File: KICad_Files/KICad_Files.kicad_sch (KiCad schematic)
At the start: 48 parts, among them J1 Conn_01x03_MountingPin, J10 Conn_01x03_Pin, J2 USB_C_Receptacle_USB2.0_14P, J3 Conn_01x03_MountingPin, J4 Conn_01x03_MountingPin, J5 Conn_01x03_Pin, J6 Conn_01x06, J7 Conn_01x06, J8 Conn_01x03_Pin, J9 Conn_01x02_Pin, SW1 Reset, SW2 Boot, U1 ESP32-C3, U2 USBLC6-2SC6, U3 TPP361061-T6TR, Y1 40.0MHz

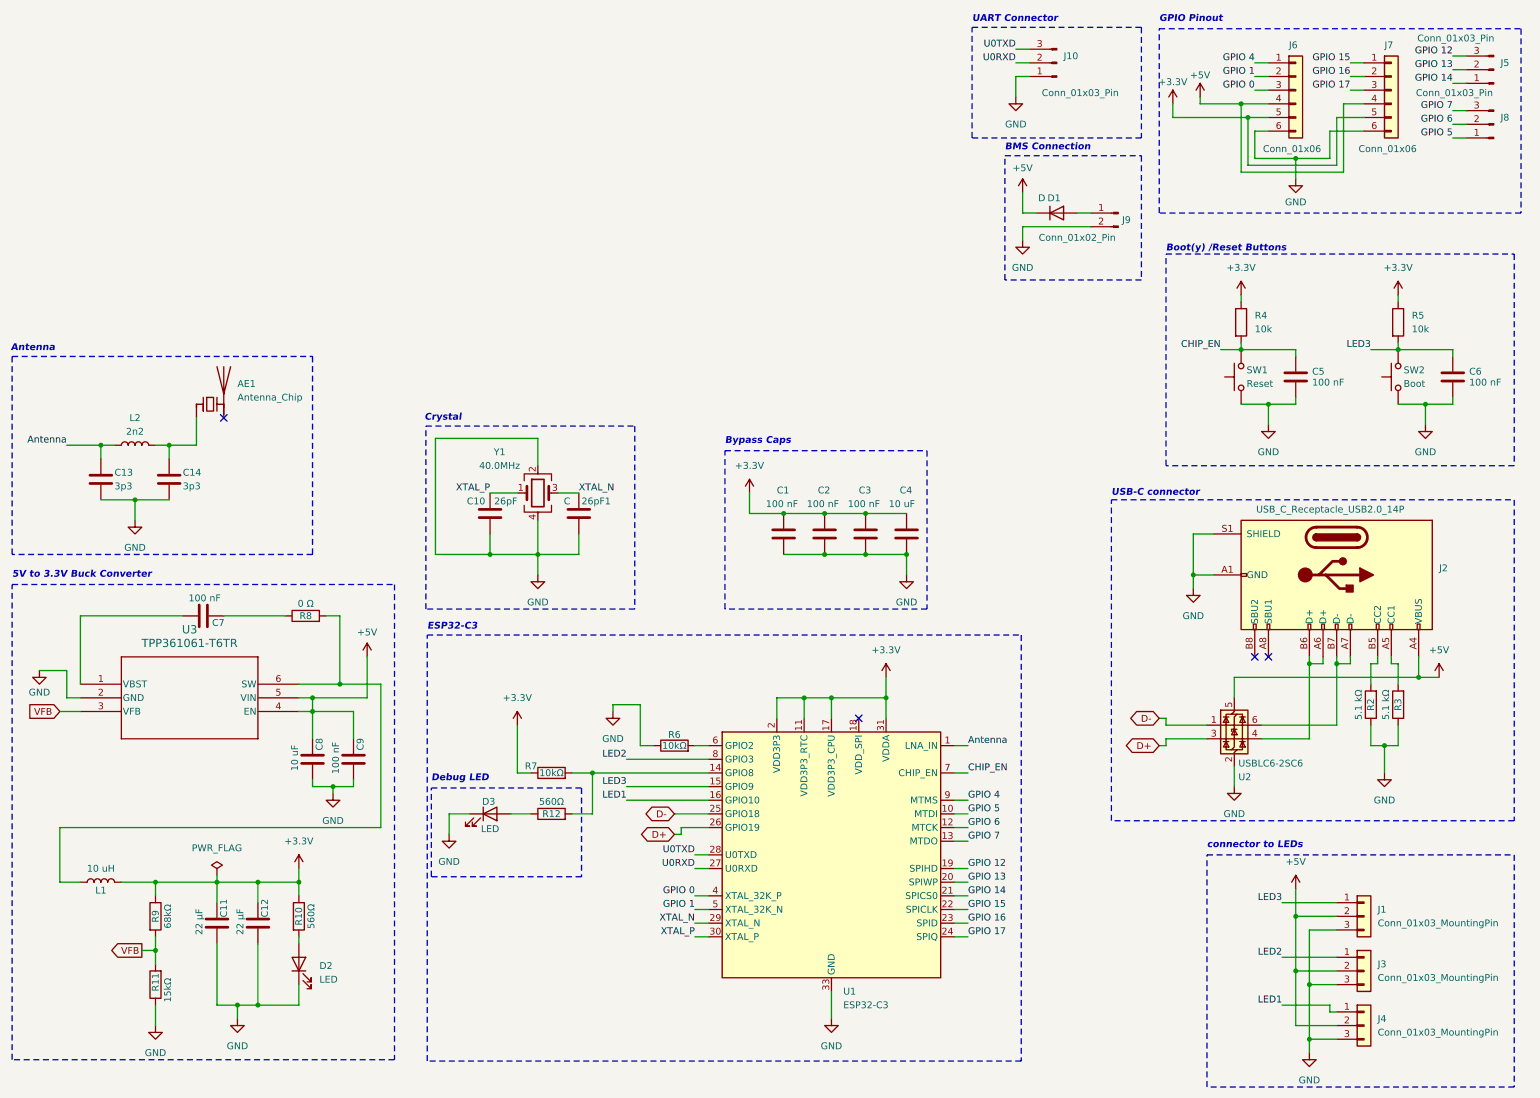
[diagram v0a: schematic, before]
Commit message: Complete rework of the PCB routing
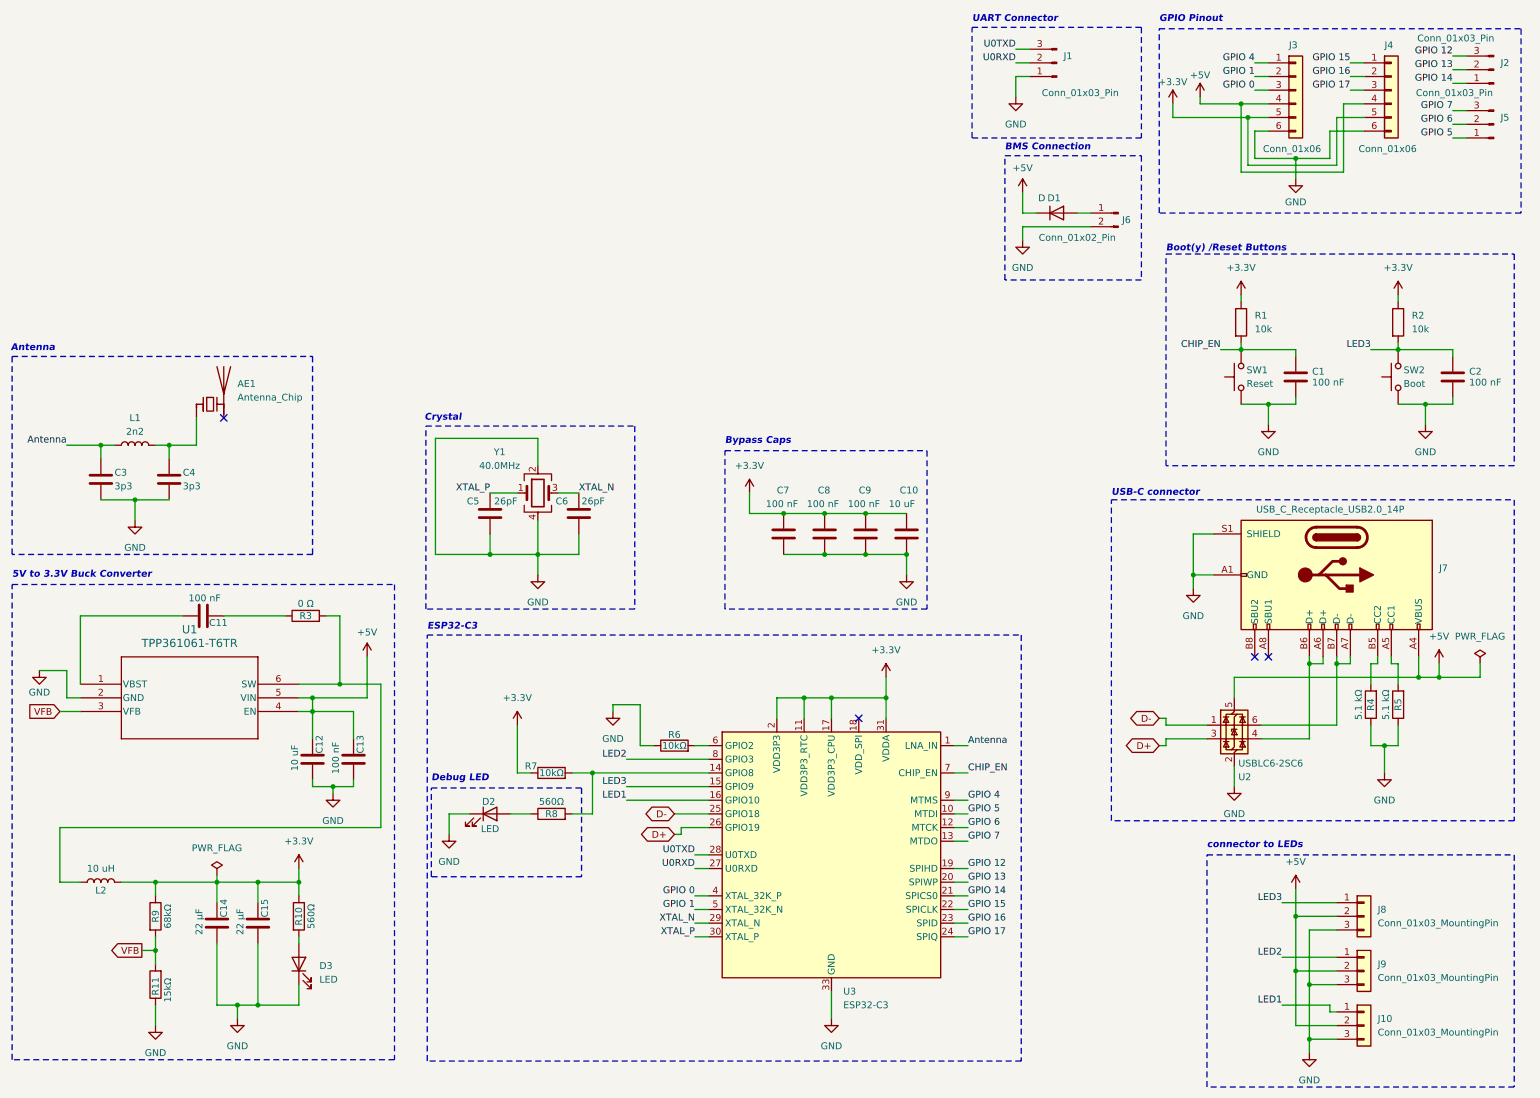
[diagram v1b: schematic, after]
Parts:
- C6: renamed from 26pF1; value C -> 26pF
- J1: renamed from J10; footprint Connector_PinHeader_2.00mm:PinHeader_1x03_P2.00mm_Vertical -> Connector_PinHeader_1.00mm:PinHeader_1x03_P1.00mm_Vertical
- J6: renamed from J9; footprint Connector_PinHeader_1.00mm:PinHeader_1x02_P1.00mm_Vertical -> Connector_PinHeader_2.00mm:PinHeader_1x02_P2.00mm_Vertical
- renumbered C5 to C1, C4 to C10, C7 to C11, C8 to C12, C9 to C13, C11 to C14, C12 to C15, C6 to C2, C13 to C3, C14 to C4, C10 to C5, C1 to C7, C2 to C8, C3 to C9, D3 to D2, D2 to D3, J4 to J10, J5 to J2, J6 to J3, J7 to J4, J8 to J5, J2 to J7, J1 to J8, J3 to J9, L2 to L1, L1 to L2, R4 to R1, R5 to R2, R8 to R3, R2 to R4, R3 to R5, R12 to R8, U3 to U1, U1 to U3

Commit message: Redesign Add 24V buck converter
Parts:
- removed C1: 100 nF, Capacitor_SMD:C_0603_1608Metric_Pad1.08x0.95mm_HandSolder, symbol Device:C
- removed C5: 26pF, Capacitor_SMD:C_0603_1608Metric_Pad1.08x0.95mm_HandSolder, symbol Device:C
- removed D1: D, Diode_SMD:D_0603_1608Metric_Pad1.05x0.95mm_HandSolder, symbol Device:D
- removed D3: LED, LED_SMD:LED_0805_2012Metric_Pad1.15x1.40mm_HandSolder, symbol Device:LED
- removed J1: Conn_01x03_Pin, Connector_PinHeader_1.00mm:PinHeader_1x03_P1.00mm_Vertical, symbol Connector:Conn_01x03_Pin
- removed J2, J5: Conn_01x03_Pin, Connector_PinHeader_2.00mm:PinHeader_1x03_P2.00mm_Vertical, symbol Connector:Conn_01x03_Pin
- removed J3, J4: Conn_01x06, Connector_PinHeader_2.00mm:PinHeader_1x06_P2.00mm_Vertical, symbol Connector_Generic:Conn_01x06
- removed J8: Conn_01x03_MountingPin, Connector_Molex:Molex_PicoBlade_53047-0310_1x03_P1.25mm_Vertical, symbol Connector_Generic:Conn_01x03
- removed R1, R2: 10k, Resistor_SMD:R_0603_1608Metric_Pad0.98x0.95mm_HandSolder, symbol Device:R
- removed SW1: Reset, Micro_button:RKB2SJK250SMTR LFS, symbol Switch:SW_Push
- removed SW2: Boot, Micro_button:RKB2SJK250SMTR LFS, symbol Switch:SW_Push
- added C10: 100n, Capacitor_SMD:C_0603_1608Metric_Pad1.08x0.95mm_HandSolder, symbol Device:C
- added C11, C3, C9: 1u, Capacitor_SMD:C_0603_1608Metric_Pad1.08x0.95mm_HandSolder, symbol Device:C
- added C19: 10pF, Capacitor_SMD:C_0402_1005Metric_Pad0.74x0.62mm_HandSolder, symbol Device:C
- added C4: 10u 35V, Capacitor_SMD:C_0603_1608Metric_Pad1.08x0.95mm_HandSolder, symbol Device:C
- added J10, J11, J13, J14, J15, J16, J17, J18, J19, J2, J20, J21, J3, J4, J5, J6, J7, J8, J9: Conn_01x06, extraFootprints:01_P2.00mm, symbol Connector_Generic:Conn_01x01
- added L2: 2n2, Inductor_SMD:L_0603_1608Metric, symbol Device:L
- added R4: 10k, Resistor_SMD:R_0603_1608Metric_Pad0.98x0.95mm_HandSolder, symbol Device:R
- added U1: MCP1703Ax-330xxTT, Package_TO_SOT_SMD:SOT-23, symbol Regulator_Linear:MCP1703Ax-330xxTT
- C1: renamed from C11; value 100 nF -> 100n
- C12: renamed from C3; value 3p3 -> 1p5; footprint Capacitor_SMD:C_0603_1608Metric_Pad1.08x0.95mm_HandSolder -> Capacitor_SMD:C_0402_1005Metric_Pad0.74x0.62mm_HandSolder
- C13: renamed from C4; value 3p3 -> 1p5; footprint Capacitor_SMD:C_0603_1608Metric_Pad1.08x0.95mm_HandSolder -> Capacitor_SMD:C_0402_1005Metric_Pad0.74x0.62mm_HandSolder
- C18: renamed from C6; value 26pF -> 10pF; footprint Capacitor_SMD:C_0603_1608Metric_Pad1.08x0.95mm_HandSolder -> Capacitor_SMD:C_0402_1005Metric_Pad0.74x0.62mm_HandSolder
- C2: value 100 nF -> 1u
- C5: renamed from C12; value 10 uF -> 10u 35V
- C6: renamed from C13; value 100 nF -> 100n 35V
- C7: renamed from C14; value 22 μF -> 22u; footprint Capacitor_SMD:C_0603_1608Metric_Pad1.08x0.95mm_HandSolder -> Capacitor_SMD:C_0805_2012Metric_Pad1.18x1.45mm_HandSolder
- C8: renamed from C15; value 22 μF -> 22u; footprint Capacitor_SMD:C_0603_1608Metric_Pad1.08x0.95mm_HandSolder -> Capacitor_SMD:C_0805_2012Metric_Pad1.18x1.45mm_HandSolder
- J1: renamed from J6; value Conn_01x02_Pin -> Power Input; footprint Connector_PinHeader_2.00mm:PinHeader_1x02_P2.00mm_Vertical -> Connector_Molex:Molex_PicoBlade_53047-0210_1x02_P1.25mm_Vertical
- J12: renamed from J7; value USB_C_Receptacle_USB2.0_14P -> USB_C_Receptacle_USB2.0_16P
- L1: renamed from L2; value 10 uH -> 10u (1276AS-H-100M=P2); footprint Inductor_SMD:L_1008_2520Metric_Pad1.43x2.20mm_HandSolder -> Inductor_SMD:L_1210_3225Metric_Pad1.42x2.65mm_HandSolder
- L3: renamed from L1; value 2n2 -> 6n2; footprint Inductor_SMD:L_0603_1608Metric -> Inductor_SMD:L_0402_1005Metric_Pad0.77x0.64mm_HandSolder
- R1: renamed from R3; value 0 Ω -> 0R
- R10: value 560Ω -> 10R
- R2: renamed from R9; value 68kΩ -> 11k
- R3: renamed from R11; value 15kΩ -> 1k5
- R7: renamed from R4; value 5.1 kΩ -> 5k1
- R8: renamed from R5; value 5.1 kΩ -> 5k1
- U2: renamed from U1; symbol TPP361061-T6TR:TPP361061-T6TR -> extraSymbols:TPP361061-T6TR
- Y1: value 40.0MHz -> E9X400081G08; footprint Crystal:Crystal_SMD_3225-4Pin_3.2x2.5mm -> Crystal:Crystal_SMD_2016-4Pin_2.0x1.6mm
- renumbered C7 to C14, C8 to C15, C9 to C16, C10 to C17, D2 to D1, J9 to J22, J10 to J23, R6 to R5, R7 to R6, R8 to R9, U2 to U3, U3 to U4
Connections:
- net +3.3V: now also R5.1, R6.2, C10.1, C3.1, L2.1, R4.1, U1.2 (VO); no longer C7.2, C8.2, L1.1, R10.1, R2.1, R6.1, U4.2 (VDD3P3), U4.3 (VDD3P3)
- net +5V: now also C2.1, C7.2, C8.2, L1.1, R2.1, U1.3 (VI); no longer C5.2, C6.2, U2.4 (EN), U2.5 (VIN)
- net GND: now also C10.2, C11.2, C19.2, C3.2, C4.1, C9.2, U1.1 (GND); no longer R5.1
- net GPIO 0: now also J21.1 (Pin_1)
- net GPIO 1: now also J20.1 (Pin_1)
- net GPIO 12: now also J23.1 (Pin_1), J18.1 (Pin_1)
- net GPIO 13: now also J22.1 (Pin_1), J16.1 (Pin_1)
- net GPIO 14: now also J14.1 (Pin_1)
- net GPIO 15: now also J11.1 (Pin_1)
- net GPIO 16: now also J9.1 (Pin_1)
- net GPIO 17: now also J7.1 (Pin_1)
- net GPIO 4: now also J15.1 (Pin_1)
- net GPIO 5: now also J13.1 (Pin_1)
- net GPIO 6: now also J10.1 (Pin_1)
- net GPIO 7: now also J8.1 (Pin_1)
- net +24V: now reaches J1.1 (Pin_1)
- net +24V: now also C5.2, C6.2, U2.5 (VIN), C4.2
- net GPIO 8: now reaches R9.2, U4.14 (GPIO8)
- net GPIO 8: now also R6.1, J6.1 (Pin_1); no longer R6.2
- net GPIO 2: now reaches R5.2, U4.6 (GPIO2)
- net GPIO 2: now also J19.1 (Pin_1)
- net at R10.2: now also Y1.1, C19.1
- net D_Raw+: now reaches J12.A6 (D+), J12.B6 (D+), U3.4 (I/O2)
- net D_Raw-: now reaches J12.A7 (D-), J12.B7 (D-), U3.6 (I/O1)
- net Antenna: no longer names the net of C12.1, L3.1, U4.1 (LNA_IN)
- net CHIP_EN: no longer names the net of U4.7 (CHIP_EN)
- net CHIP_EN: now also C9.1, R4.2
- net LED1 renamed GPIO 10
- net GPIO 10: now also J2.1 (Pin_1); no longer J23.1 (Pin_1)
- net LED2 renamed GPIO 3
- net GPIO 3: now also J17.1 (Pin_1); no longer J22.1 (Pin_1)
- net LED3 renamed GPIO 9
- net GPIO 9: now also J4.1 (Pin_1); no longer C2.1
- net U0RXD renamed U0RXD/GPIO 20
- net U0RXD/GPIO 20: now also J5.1 (Pin_1)
- net U0TXD renamed U0TXD/GPIO 21
- net U0TXD/GPIO 21: now also J3.1 (Pin_1)
- net VFB: no longer names the net of R2.2, R3.2, U2.3 (VFB)
- net XTAL_N: no longer names the net of C18.1, U4.29 (XTAL_N), Y1.3
- net XTAL_P: no longer names the net of U4.30 (XTAL_P)
- net XTAL_P: now also R10.1; no longer Y1.1
- new net: C11.1, L2.2, U4.2 (VDD3P3), U4.3 (VDD3P3)
- no-connect marks 4 -> 5
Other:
- note added: "24V power input"
- note added: "24V to 5V buck converter"
- note added: "5V to 3.3V LDO"
- note removed: "5V to 3.3V Buck Converter"
- note removed: "BMS Connection"
- note removed: "Boot(y) /Reset Buttons"
- note removed: "UART Connector"
- moved on the sheet: AE1, C1, C12, C13, C14, C15, C16, C17, C18, C5, C6, C7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
